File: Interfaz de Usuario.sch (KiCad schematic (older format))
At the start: 8 parts, among them J2 Conn_02x14_Odd_Even, J3 Conn_01x04_Male, SW1 SW_Push_Dual

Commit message: Issue #1: Correción de las conexiones Bus
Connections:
- net labels added: DTR, MCU_PA0, MCU_PA1, MCU_PA2, MCU_PA[0..2], MCU_PB11, MCU_PB13, MCU_PB14, MCU_PB7, MCU_PB8, MCU_PC0, MCU_PC1, MCU_PC13, MCU_PC14, MCU_PC15, MCU_PD4, MCU_PD5, MCU_PD6, MCU_PE10, MCU_PE11, MCU_PE12, MCU_PE13, MCU_PF0, MCU_PF1, MCU_PF2
- net labels removed: DRT, MCU_PA[0..3]
- wire segments 47 -> 46
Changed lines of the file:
@@
 DSR
 Text HLabel 9350 4750 2    43   BiDi ~ 0
-DRT
+DTR
 Text HLabel 9350 4650 2    43   BiDi ~ 0
 CD
@@
 $EndComp
 Text HLabel 7150 1675 0    43   BiDi ~ 0
-MCU_PA[0..3]
+MCU_PA[0..2]
 Text HLabel 7150 1875 0    43   BiDi ~ 0
 MCU_PB[7..14]
 Text HLabel 9625 2925 2    43   BiDi ~ 0
-MCU_PC[0..15]
+MCU_PF[0..2]
 Text HLabel 9625 3350 2    43   BiDi ~ 0
 MCU_PD[4..7]
@@
 MCU_PE[10..13]
 Text HLabel 9625 3125 2    43   BiDi ~ 0
-MCU_PF[0..2]
+MCU_PC[0..15]
 Wire Wire Line
 	8200 1750 8150 1750
@@
 	9050 2750 9150 2850
 Wire Wire Line
-	8150 1750 8150 1850
-Wire Wire Line
 	8200 1850 8150 1850
-Connection ~ 8150 1850
 Wire Wire Line
 	8150 1850 8150 3325
@@
 Wire Wire Line
 	2625 4700 2625 4875
-Text HLabel 3025 3600 2    43   BiDi ~ 0
-MCU_PD[4..7]
-Wire Wire Line
-	3025 3600 2625 3600
 Wire Wire Line
 	2625 3600 2625 3925
-Text Label 2625 3600 0    43   ~ 0
+Text Label 2925 3600 0    43   ~ 0
 MCU_PD7
 $Comp
@@
 Text Notes 8275 3775 0    43   ~ 0
 Pines GPIOs
+Text Label 7800 1950 0    43   ~ 0
+MCU_PA0
+Text Label 7800 2050 0    43   ~ 0
+MCU_PA1
+Text Label 7800 2150 0    43   ~ 0
+MCU_PA2
+Text Label 7800 2250 0    43   ~ 0
+MCU_PB7
+Text Label 7800 2350 0    43   ~ 0
+MCU_PB8
+Text Label 7750 2450 0    43   ~ 0
+MCU_PB11
+Text Label 7750 2550 0    43   ~ 0
+MCU_PB13
+Text Label 7750 2750 0    43   ~ 0
+MCU_PE10
+Text Label 7750 2850 0    43   ~ 0
+MCU_PE11
+Text Label 7750 2950 0    43   ~ 0
+MCU_PE12
+Text Label 7750 3050 0    43   ~ 0
+MCU_PE13
+Text Label 8800 1950 0    43   ~ 0
+MCU_PF0
+Text Label 8800 2050 0    43   ~ 0
+MCU_PF1
+Text Label 8800 2150 0    43   ~ 0
+MCU_PF2
+Text Label 7750 2650 0    43   ~ 0
+MCU_PB14
+Text Label 8800 2250 0    43   ~ 0
+MCU_PC0
+Text Label 8800 2350 0    43   ~ 0
+MCU_PC1
+Text Label 8800 2450 0    43   ~ 0
+MCU_PC13
+Text Label 8800 2550 0    43   ~ 0
+MCU_PC14
+Text Label 8800 2650 0    43   ~ 0
+MCU_PC15
+Text Label 8800 2750 0    43   ~ 0
+MCU_PD4
+Text Label 8800 2850 0    43   ~ 0
+MCU_PD5
+Text Label 8800 2950 0    43   ~ 0
+MCU_PD6
+Text Label 8800 3050 0    43   ~ 0
+MCU_PD7
+Wire Wire Line
+	2625 3600 2925 3600
 Wire Bus Line
 	7675 1675 7675 2050
@@
 Wire Bus Line
 	7500 1875 7500 2550
+Text HLabel 8150 1750 0    43   Output ~ 0
+MCU_RESET
 $EndSCHEMATC

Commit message: Issue #1: Cambio de conector USB-UART
Se agrega un conector para todos los pines UART ofrecidos por el IC
XR21B1411 de Maxlinear.
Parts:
- removed J3: Conn_01x04_Male, symbol Connector:Conn_01x04_Male
- added J3: Conn_02x04_Odd_Even, symbol Connector_Generic:Conn_02x04_Odd_Even
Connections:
- net labels added: CTS, RTS, RX, TX
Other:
- note added: "Pines USB-UART\n"
- note removed: "Pines "sobrantes" de USB-UART\n(definir si es necesario dejarlos disponibles)"
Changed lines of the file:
@@
 	1    0    0    -1
 $EndComp
-$Comp
-L Connector:Conn_01x04_Male J3
-U 1 1 5F5DBD3C
-P 9150 4650
-F 0 "J3" H 9258 4931 50  0000 C CNN
-F 1 "Conn_01x04_Male" H 9258 4840 50  0000 C CNN
-F 2 "" H 9150 4650 50  0001 C CNN
-F 3 "~" H 9150 4650 50  0001 C CNN
-	1    9150 4650
-	1    0    0    -1
-$EndComp
-Text Notes 8700 5175 0    43   ~ 0
-Pines "sobrantes" de USB-UART\n(definir si es necesario dejarlos disponibles)
+Text Notes 8800 5125 0    43   ~ 0
+Pines USB-UART\n
 $Comp
 L Connector_Generic:Conn_02x14_Odd_Even J2
@@
 Wire Wire Line
 	2625 3600 2925 3600
-Wire Bus Line
-	7675 1675 7675 2050
-Wire Bus Line
-	9500 2050 9500 2925
-Wire Bus Line
-	9325 2350 9325 3125
-Wire Bus Line
-	9150 2850 9150 3350
-Wire Bus Line
-	7325 2075 7325 2950
-Wire Bus Line
-	7500 1875 7500 2550
 Text HLabel 8150 1750 0    43   Output ~ 0
 MCU_RESET
+Wire Bus Line
+	7675 1675 7675 2050
+Wire Bus Line
+	9500 2050 9500 2925
+Wire Bus Line
+	9325 2350 9325 3125
+Wire Bus Line
+	9150 2850 9150 3350
+Wire Bus Line
+	7325 2075 7325 2950
+Wire Bus Line
+	7500 1875 7500 2550
+$Comp
+L Connector_Generic:Conn_02x04_Odd_Even J3
+U 1 1 5F5CD54F
+P 9050 4650
+F 0 "J3" H 9100 4967 50  0000 C CNN
+F 1 "Conn_02x04_Odd_Even" H 9100 4876 50  0000 C CNN
+F 2 "" H 9050 4650 50  0001 C CNN
+F 3 "~" H 9050 4650 50  0001 C CNN
+	1    9050 4650
+	1    0    0    -1
+$EndComp
+Text HLabel 8850 4550 0    43   Input ~ 0
+RX
+Text HLabel 8850 4650 0    43   Output ~ 0
+TX
+Text HLabel 8850 4750 0    43   BiDi ~ 0
+CTS
+Text HLabel 8850 4850 0    43   BiDi ~ 0
+RTS
 $EndSCHEMATC

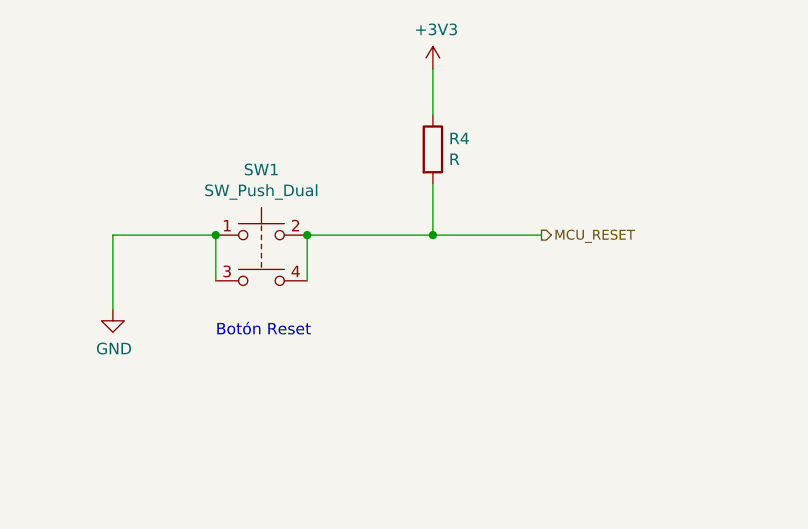
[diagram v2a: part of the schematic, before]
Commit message: Issue #1: Mejora de la funcionalidad de reset
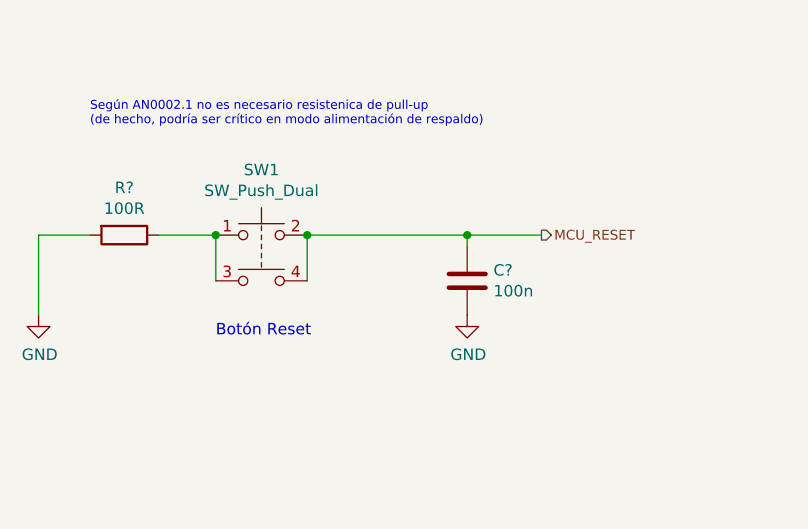
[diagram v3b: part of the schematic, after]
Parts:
- removed R4: R, symbol Device:R
- added C?: 100n, symbol Device:C
- added R?: 100R, symbol Device:R
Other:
- note added: "Según AN0002.1 no es necesario resistenica de pull-up\n(de hecho, podría ser crítico en modo alimentación de respaldo)"
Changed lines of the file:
@@
 L power:GND #PWR015
 U 1 1 5F61A6A2
-P 1375 2275
-F 0 "#PWR015" H 1375 2025 50  0001 C CNN
-F 1 "GND" H 1380 2102 50  0000 C CNN
-F 2 "" H 1375 2275 50  0001 C CNN
-F 3 "" H 1375 2275 50  0001 C CNN
-	1    1375 2275
+P 1050 2300
+F 0 "#PWR015" H 1050 2050 50  0001 C CNN
+F 1 "GND" H 1055 2127 50  0000 C CNN
+F 2 "" H 1050 2300 50  0001 C CNN
+F 3 "" H 1050 2300 50  0001 C CNN
+	1    1050 2300
 	1    0    0    -1
 $EndComp
-$Comp
-L Device:R R4
-U 1 1 5F61AD2C
-P 2775 1575
-F 0 "R4" H 2845 1621 50  0000 L CNN
-F 1 "R" H 2845 1530 50  0000 L CNN
-F 2 "" V 2705 1575 50  0001 C CNN
-F 3 "~" H 2775 1575 50  0001 C CNN
-	1    2775 1575
-	1    0    0    -1
-$EndComp
-$Comp
-L power:+3V3 #PWR019
-U 1 1 5F61B478
-P 2775 1225
-F 0 "#PWR019" H 2775 1075 50  0001 C CNN
-F 1 "+3V3" H 2790 1398 50  0000 C CNN
-F 2 "" H 2775 1225 50  0001 C CNN
-F 3 "" H 2775 1225 50  0001 C CNN
-	1    2775 1225
-	1    0    0    -1
-$EndComp
-Wire Wire Line
-	2225 1950 2775 1950
-Wire Wire Line
-	2775 1725 2775 1950
-Connection ~ 2775 1950
-Wire Wire Line
-	2775 1950 3250 1950
 Wire Wire Line
 	2225 1950 2225 2150
 Connection ~ 2225 1950
 Wire Wire Line
-	1825 1950 1375 1950
-Wire Wire Line
-	1375 1950 1375 2275
-Wire Wire Line
 	1825 1950 1825 2150
-Connection ~ 1825 1950
-Wire Wire Line
-	2775 1225 2775 1425
 Text Notes 8275 3775 0    43   ~ 0
 Pines GPIOs
@@
 Text HLabel 8150 1750 0    43   Output ~ 0
 MCU_RESET
-Wire Bus Line
-	7675 1675 7675 2050
-Wire Bus Line
-	9500 2050 9500 2925
-Wire Bus Line
-	9325 2350 9325 3125
-Wire Bus Line
-	9150 2850 9150 3350
-Wire Bus Line
-	7325 2075 7325 2950
-Wire Bus Line
-	7500 1875 7500 2550
 $Comp
 L Connector_Generic:Conn_02x04_Odd_Even J3
@@
 Text HLabel 8850 4850 0    43   BiDi ~ 0
 RTS
+Text Notes 1275 1475 0    39   ~ 0
+Según AN0002.1 no es necesario resistenica de pull-up\n(de hecho, podría ser crítico en modo alimentación de respaldo)
+$Comp
+L Device:C C?
+U 1 1 5F608348
+P 2925 2150
+F 0 "C?" H 3040 2196 50  0000 L CNN
+F 1 "100n" H 3040 2105 50  0000 L CNN
+F 2 "" H 2963 2000 50  0001 C CNN
+F 3 "~" H 2925 2150 50  0001 C CNN
+	1    2925 2150
+	1    0    0    -1
+$EndComp
+$Comp
+L power:GND #PWR?
+U 1 1 5F608A3C
+P 2925 2300
+F 0 "#PWR?" H 2925 2050 50  0001 C CNN
+F 1 "GND" H 2930 2127 50  0000 C CNN
+F 2 "" H 2925 2300 50  0001 C CNN
+F 3 "" H 2925 2300 50  0001 C CNN
+	1    2925 2300
+	1    0    0    -1
+$EndComp
+$Comp
+L Device:R R?
+U 1 1 5F60A43B
+P 1425 1950
+F 0 "R?" V 1218 1950 50  0000 C CNN
+F 1 "100R" V 1309 1950 50  0000 C CNN
+F 2 "" V 1355 1950 50  0001 C CNN
+F 3 "~" H 1425 1950 50  0001 C CNN
+	1    1425 1950
+	0    1    1    0
+$EndComp
+Wire Wire Line
+	1050 1950 1275 1950
+Wire Wire Line
+	1575 1950 1825 1950
+Connection ~ 1825 1950
+Wire Wire Line
+	2225 1950 2925 1950
+Wire Wire Line
+	2925 2000 2925 1950
+Connection ~ 2925 1950
+Wire Wire Line
+	2925 1950 3250 1950
+Wire Wire Line
+	1050 1950 1050 2300
+Wire Bus Line
+	7675 1675 7675 2050
+Wire Bus Line
+	9500 2050 9500 2925
+Wire Bus Line
+	9325 2350 9325 3125
+Wire Bus Line
+	9150 2850 9150 3350
+Wire Bus Line
+	7325 2075 7325 2950
+Wire Bus Line
+	7500 1875 7500 2550
 $EndSCHEMATC

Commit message: Issue #1: Cambio de conector GPIOs
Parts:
- removed J2: Conn_02x14_Odd_Even, symbol Connector_Generic:Conn_02x14_Odd_Even
- added J2, J?: Conn_01x14, symbol Connector_Generic:Conn_01x14
- gave numbers to parts that had none: 2
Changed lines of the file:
@@
 Pines USB-UART\n
-$Comp
-L Connector_Generic:Conn_02x14_Odd_Even J2
-U 1 1 5F5DF1D0
-P 8400 2350
-F 0 "J2" H 8450 3167 50  0000 C CNN
-F 1 "Conn_02x14_Odd_Even" H 8450 3076 50  0000 C CNN
-F 2 "" H 8400 2350 50  0001 C CNN
-F 3 "~" H 8400 2350 50  0001 C CNN
-	1    8400 2350
-	1    0    0    -1
-$EndComp
 $Comp
 L power:+3V3 #PWR021
@@
 L power:GND #PWR020
 U 1 1 5F5E1C7B
-P 8150 3325
-F 0 "#PWR020" H 8150 3075 50  0001 C CNN
-F 1 "GND" H 8155 3152 50  0000 C CNN
-F 2 "" H 8150 3325 50  0001 C CNN
-F 3 "" H 8150 3325 50  0001 C CNN
-	1    8150 3325
-	1    0    0    -1
-$EndComp
-Text HLabel 7150 1675 0    43   BiDi ~ 0
+P 7775 3325
+F 0 "#PWR020" H 7775 3075 50  0001 C CNN
+F 1 "GND" H 7780 3152 50  0000 C CNN
+F 2 "" H 7775 3325 50  0001 C CNN
+F 3 "" H 7775 3325 50  0001 C CNN
+	1    7775 3325
+	1    0    0    -1
+$EndComp
+Text HLabel 6775 1675 0    43   BiDi ~ 0
 MCU_PA[0..2]
-Text HLabel 7150 1875 0    43   BiDi ~ 0
+Text HLabel 6775 1875 0    43   BiDi ~ 0
 MCU_PB[7..14]
 Text HLabel 9625 2925 2    43   BiDi ~ 0
@@
 Text HLabel 9625 3350 2    43   BiDi ~ 0
 MCU_PD[4..7]
-Text HLabel 7150 2075 0    43   BiDi ~ 0
+Text HLabel 6775 2075 0    43   BiDi ~ 0
 MCU_PE[10..13]
 Text HLabel 9625 3125 2    43   BiDi ~ 0
 MCU_PC[0..15]
 Wire Wire Line
-	8200 1750 8150 1750
+	7825 1750 7775 1750
 Wire Wire Line
 	8700 1750 9050 1750
@@
 	9450 1850 9450 1300
 Wire Wire Line
-	8200 1950 7775 1950
-Wire Wire Line
-	8200 2050 7775 2050
-Wire Wire Line
-	8200 2150 7775 2150
-Entry Wire Line
-	7775 1950 7675 1850
-Entry Wire Line
-	7775 2050 7675 1950
-Entry Wire Line
-	7775 2150 7675 2050
-Entry Wire Line
-	7600 2250 7500 2150
-Entry Wire Line
-	7600 2350 7500 2250
-Entry Wire Line
-	7600 2450 7500 2350
-Entry Wire Line
-	7600 2550 7500 2450
-Entry Wire Line
-	7600 2650 7500 2550
-Wire Wire Line
-	7600 2250 8200 2250
-Wire Wire Line
-	7600 2350 8200 2350
-Wire Wire Line
-	7600 2450 8200 2450
-Wire Wire Line
-	7600 2550 8200 2550
-Wire Wire Line
-	7600 2650 8200 2650
-Wire Bus Line
-	7150 2075 7325 2075
-Wire Bus Line
-	7150 1875 7500 1875
-Wire Bus Line
-	7150 1675 7675 1675
-Entry Wire Line
-	7425 2750 7325 2650
-Entry Wire Line
-	7425 2850 7325 2750
-Entry Wire Line
-	7425 2950 7325 2850
-Entry Wire Line
-	7425 3050 7325 2950
-Wire Wire Line
-	7425 3050 8200 3050
-Wire Wire Line
-	7425 2950 8200 2950
-Wire Wire Line
-	7425 2850 8200 2850
-Wire Wire Line
-	7425 2750 8200 2750
+	7825 1950 7400 1950
+Wire Wire Line
+	7825 2050 7400 2050
+Wire Wire Line
+	7825 2150 7400 2150
+Entry Wire Line
+	7400 1950 7300 1850
+Entry Wire Line
+	7400 2050 7300 1950
+Entry Wire Line
+	7400 2150 7300 2050
+Entry Wire Line
+	7225 2250 7125 2150
+Entry Wire Line
+	7225 2350 7125 2250
+Entry Wire Line
+	7225 2450 7125 2350
+Entry Wire Line
+	7225 2550 7125 2450
+Entry Wire Line
+	7225 2650 7125 2550
+Wire Wire Line
+	7225 2250 7825 2250
+Wire Wire Line
+	7225 2350 7825 2350
+Wire Wire Line
+	7225 2450 7825 2450
+Wire Wire Line
+	7225 2550 7825 2550
+Wire Wire Line
+	7225 2650 7825 2650
+Wire Bus Line
+	6775 2075 6950 2075
+Wire Bus Line
+	6775 1875 7125 1875
+Wire Bus Line
+	6775 1675 7300 1675
+Entry Wire Line
+	7050 2750 6950 2650
+Entry Wire Line
+	7050 2850 6950 2750
+Entry Wire Line
+	7050 2950 6950 2850
+Entry Wire Line
+	7050 3050 6950 2950
+Wire Wire Line
+	7050 3050 7825 3050
+Wire Wire Line
+	7050 2950 7825 2950
+Wire Wire Line
+	7050 2850 7825 2850
+Wire Wire Line
+	7050 2750 7825 2750
 Wire Wire Line
 	8700 2750 9050 2750
@@
 	9050 2750 9150 2850
 Wire Wire Line
-	8200 1850 8150 1850
-Wire Wire Line
-	8150 1850 8150 3325
+	7825 1850 7775 1850
+Wire Wire Line
+	7775 1850 7775 3325
 Entry Wire Line
 	9325 2350 9225 2250
@@
 Text Notes 8275 3775 0    43   ~ 0
 Pines GPIOs
-Text Label 7800 1950 0    43   ~ 0
+Text Label 7425 1950 0    43   ~ 0
 MCU_PA0
-Text Label 7800 2050 0    43   ~ 0
+Text Label 7425 2050 0    43   ~ 0
 MCU_PA1
-Text Label 7800 2150 0    43   ~ 0
+Text Label 7425 2150 0    43   ~ 0
 MCU_PA2
-Text Label 7800 2250 0    43   ~ 0
+Text Label 7425 2250 0    43   ~ 0
 MCU_PB7
-Text Label 7800 2350 0    43   ~ 0
+Text Label 7425 2350 0    43   ~ 0
 MCU_PB8
-Text Label 7750 2450 0    43   ~ 0
+Text Label 7375 2450 0    43   ~ 0
 MCU_PB11
-Text Label 7750 2550 0    43   ~ 0
+Text Label 7375 2550 0    43   ~ 0
 MCU_PB13
-Text Label 7750 2750 0    43   ~ 0
+Text Label 7375 2750 0    43   ~ 0
 MCU_PE10
-Text Label 7750 2850 0    43   ~ 0
+Text Label 7375 2850 0    43   ~ 0
 MCU_PE11
-Text Label 7750 2950 0    43   ~ 0
+Text Label 7375 2950 0    43   ~ 0
 MCU_PE12
-Text Label 7750 3050 0    43   ~ 0
+Text Label 7375 3050 0    43   ~ 0
 MCU_PE13
 Text Label 8800 1950 0    43   ~ 0
@@
 Text Label 8800 2150 0    43   ~ 0
 MCU_PF2
-Text Label 7750 2650 0    43   ~ 0
+Text Label 7375 2650 0    43   ~ 0
 MCU_PB14
 Text Label 8800 2250 0    43   ~ 0
@@
 Wire Wire Line
 	2625 3600 2925 3600
-Text HLabel 8150 1750 0    43   Output ~ 0
+Text HLabel 7775 1750 0    43   Output ~ 0
 MCU_RESET
 $Comp
@@
 Según AN0002.1 no es necesario resistenica de pull-up\n(de hecho, podría ser crítico en modo alimentación de respaldo)
 $Comp
-L Device:C C?
+L Device:C C3
 U 1 1 5F608348
 P 2925 2150
-F 0 "C?" H 3040 2196 50  0000 L CNN
+F 0 "C3" H 3040 2196 50  0000 L CNN
 F 1 "100n" H 3040 2105 50  0000 L CNN
 F 2 "" H 2963 2000 50  0001 C CNN
@@
 $EndComp
 $Comp
-L power:GND #PWR?
+L power:GND #PWR0101
 U 1 1 5F608A3C
 P 2925 2300
-F 0 "#PWR?" H 2925 2050 50  0001 C CNN
+F 0 "#PWR0101" H 2925 2050 50  0001 C CNN
 F 1 "GND" H 2930 2127 50  0000 C CNN
 F 2 "" H 2925 2300 50  0001 C CNN
@@
 $EndComp
 $Comp
-L Device:R R?
+L Device:R R4
 U 1 1 5F60A43B
 P 1425 1950
-F 0 "R?" V 1218 1950 50  0000 C CNN
+F 0 "R4" V 1218 1950 50  0000 C CNN
 F 1 "100R" V 1309 1950 50  0000 C CNN
 F 2 "" V 1355 1950 50  0001 C CNN
@@
 Wire Wire Line
 	1050 1950 1050 2300
-Wire Bus Line
-	7675 1675 7675 2050
+$Comp
+L Connector_Generic:Conn_01x14 J2
+U 1 1 5F616B2C
+P 8025 2350
+F 0 "J2" H 7975 3225 50  0000 L CNN
+F 1 "Conn_01x14" H 7700 3100 50  0000 L CNN
+F 2 "" H 8025 2350 50  0001 C CNN
+F 3 "~" H 8025 2350 50  0001 C CNN
+	1    8025 2350
+	1    0    0    -1
+$EndComp
+$Comp
+L Connector_Generic:Conn_01x14 J?
+U 1 1 5F61A09A
+P 8500 2350
+F 0 "J?" H 8450 3225 50  0000 C CNN
+F 1 "Conn_01x14" H 8418 3076 50  0000 C CNN
+F 2 "" H 8500 2350 50  0001 C CNN
+F 3 "~" H 8500 2350 50  0001 C CNN
+	1    8500 2350
+	-1   0    0    -1
+$EndComp
+Wire Bus Line
+	7300 1675 7300 2050
 Wire Bus Line
 	9500 2050 9500 2925
@@
 	9150 2850 9150 3350
 Wire Bus Line
-	7325 2075 7325 2950
-Wire Bus Line
-	7500 1875 7500 2550
+	6950 2075 6950 2950
+Wire Bus Line
+	7125 1875 7125 2550
 $EndSCHEMATC
